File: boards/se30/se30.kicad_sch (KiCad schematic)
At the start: 42 parts, among them J3 Conn_02x05_Odd_Even, U1 ENC624J600-PT, U2 GAL16V8, U3 GAL16V8, U4 SST39SF010, U5 LD1117S33TR_SOT223, Y1 25MHz

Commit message: Rev1 hardware
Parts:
- removed C14: 1uF, Capacitor_SMD:C_0805_2012Metric_Pad1.18x1.45mm_HandSolder, symbol Device:C
- removed U2, U3: GAL16V8, Package_LCC:PLCC-20_THT-Socket, symbol Logic_Programmable:GAL16V8
- added C15 (x4): 1uF, Capacitor_SMD:C_0805_2012Metric_Pad1.18x1.45mm_HandSolder, symbol Device:C
- added H1, H2: MountingHole, MountingHole:MountingHole_5mm, symbol Mechanical:MountingHole
- added J3: Conn_01x07, Connector_PinHeader_2.54mm:PinHeader_1x07_P2.54mm_Vertical, symbol Connector_Generic:Conn_01x07
- added TP1, TP2, TP3, TP4, TP5, TP6: TestPoint, TestPoint:TestPoint_Pad_D1.0mm, symbol Connector:TestPoint
- added U3: 74LVC2G17, Package_TO_SOT_SMD:SOT-363_SC-70-6, symbol 74xGxx:74LVC2G17
- added U4: ATF1502AS-xAx44, Package_QFP:TQFP-44_10x10mm_P0.8mm, symbol CPLD_Microchip:ATF1502AS-xAx44
- C10, C7, C8, C9: Digikey C0805C104M5RAC7800 -> 399-C0805C104M5RAC7800CT-ND; LCSC (none) -> C49678
- C10: renamed from C13; Digikey 293D106X0010A2TE3 -> 718-1118-1-ND; LCSC (none) -> C7171
- C11, C13, C15: Digikey CL21B105KAFNNNE -> 1276-1066-1-ND; LCSC (none) -> C28323
- C12: renamed from C15; Digikey C0805C682K5RAC7800 -> 399-C0805C682K5RAC7800CT-ND; LCSC (none) -> C1755
- C16: renamed from C17; Digikey C0805C103K5RAC7800 -> 399-C0805C103K5RACTUCT-ND; LCSC (none) -> C1710
- C20: renamed from C18; footprint Capacitor_SMD:C_0805_2012Metric_Pad1.18x1.45mm_HandSolder -> Capacitor_SMD:C_1206_3216Metric_Pad1.33x1.80mm_HandSolder; Digikey C0805X102K102T -> 4587-C1206X102K202TCT-ND; LCSC (none) -> C282813
- C22: renamed from C19; Digikey C0805C104M5RAC7800 -> 399-C0805C104M5RAC7800CT-ND; LCSC (none) -> C49678
- C23: renamed from C20; Digikey 293D106X0010A2TE3 -> 718-1118-1-ND; LCSC (none) -> C7171
- C5: renamed from C16; Digikey C0805C103K5RAC7800 -> 399-C0805C103K5RACTUCT-ND; LCSC (none) -> C1710
- C5, C6: Digikey C0805C180K5GAC7800 -> 399-C0805C180K5GAC7800CT-ND; LCSC (none) -> C1797
- C9: renamed from C14; Digikey C0805C682K5RAC7800 -> 399-C0805C682K5RAC7800CT-ND; LCSC (none) -> C1755
- FB1: Digikey CB05YTYH331 -> 240-2549-1-ND; LCSC (none) -> C1015
- J3: Digikey 302-S101 -> ED1543-ND; LCSC (none) -> C17179451
- JP1: renamed from JP2; footprint Jumper:SolderJumper-2_P1.3mm_Open_RoundedPad1.0x1.5mm -> Connector_PinHeader_2.54mm:PinHeader_1x02_P2.54mm_Vertical; now left out of the parts list
- JP2: renamed from JP1; footprint Jumper:SolderJumper-2_P1.3mm_Open_RoundedPad1.0x1.5mm -> Connector_PinHeader_2.54mm:PinHeader_1x02_P2.54mm_Vertical; now left out of the parts list
- R1: Digikey RMCF0805FT12K4 -> RMCF0805FT12K4CT-ND; LCSC (none) -> C317429
- R1, R2: Digikey RMCF0805FT10K0 -> RMCF0805FT10K0CT-ND; LCSC (none) -> C17414
- R2: renamed from R9; Digikey RMCF0805FT49R9 -> RMCF0805FT49R9CT-ND; LCSC (none) -> C17720
- R3: renamed from R2; Digikey RMCF0805FT10K0 -> RMCF0805FT10K0CT-ND; LCSC (none) -> C17414
- R4: renamed from R8; Digikey RMCF0805FT49R9 -> RMCF0805FT49R9CT-ND; LCSC (none) -> C17720
- R5: renamed from R6; Digikey RMCF0805FT49R9 -> RMCF0805FT49R9CT-ND; LCSC (none) -> C17720
- R6: renamed from R7; Digikey RMCF0805FT10R0 -> RMCF0805FT10R0CT-ND; LCSC (none) -> C17415
- R7: renamed from R4; Digikey RMCF0805FT49R9 -> RMCF0805FT49R9CT-ND; LCSC (none) -> C17720
- R8: renamed from R11; Digikey RMCF0805FT75R0 -> RMCF0805FT75R0CT-ND; LCSC (none) -> C2933566
- R9: renamed from R10; Digikey RMCF0805FT75R0 -> RMCF0805FT75R0CT-ND; LCSC (none) -> C2933566
- TR1: LCSC (none) -> C510548
- U2: renamed from U1; LCSC (none) -> C630732
- U4: footprint Package_LCC:PLCC-32_THT-Socket -> Package_SO:TSOP-I-32_14.4x8mm_P0.5mm; symbol Memory_Flash:SST39SF010 -> PDS-Ethernet:SST39SF010-TSOP32; Digikey PLCC-32-AT -> SST39SF010A-70-4C-WHE-ND; Digikey 2 SST39SF010A-55-4C-NHE -> (none); LCSC (none) -> C633793
- U5: Digikey LD1117S33TR -> 497-1242-1-ND; LCSC (none) -> C6186
- Y1: Digikey 2151-RH100-25.000-18-F-1020-EXT-TRDKR-ND -> 2151-RH100-25.000-18-F-1020-EXT-TRCT-ND; LCSC (none) -> C9006
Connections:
- net +3.3V: no longer R3.1
- net +5V: now also U4.8 (VCC), C15.1, C15.1, C15.1, C15.1, J3.5 (Pin_5), U3.5 (VCC), U4.17 (VCC), U4.29 (VCC), U4.41 (VCC), U4.9 (VCC); no longer U4.32 (VCC)
- net A0: now also U4.20 (A0), U4.3 (I/O); no longer U4.12 (A0)
- net A1: now also U4.19 (A1); no longer U4.11 (A1)
- net A10: now also U4.31 (A10); no longer U4.23 (A10)
- net A11: now also U4.1 (A11); no longer U4.25 (A11)
- net A12: now also U4.12 (A12); no longer U4.4 (A12)
- net A13: now also U4.4 (A13); no longer U4.28 (A13)
- net A14: now also U4.5 (A14); no longer U4.29 (A14)
- net A15: now also U4.11 (A15); no longer U4.3 (A15)
- net A16: now also U4.12 (I/O)
- net A2: now also U4.18 (A2); no longer U4.10 (A2)
- net A24: now also U4.13 (I/O)
- net A25: now also U4.14 (I/O)
- net A26: now also U4.15 (I/O)
- net A27: now also U4.18 (I/O)
- net A28: now also U4.19 (I/O/PD2)
- net A29: now also U4.20 (I/O)
- net A3: now also U4.17 (A3); no longer U4.9 (A3)
- net A30: now also U4.21 (I/O)
- net A31: now also U4.22 (I/O)
- net A4: now also U4.16 (A4); no longer U4.8 (A4)
- net A5: now also U4.15 (A5); no longer U4.7 (A5)
- net A6: now also U4.14 (A6); no longer U4.6 (A6)
- net A7: now also U4.13 (A7); no longer U4.5 (A7)
- net A8: now also U4.3 (A8); no longer U4.27 (A8)
- net A9: now also U4.2 (A9); no longer U4.26 (A9)
- net B0SEL: now also TP3.1, U3.3, U4.6 (I/O); no longer U2.50 (WR/WRL/B0SEL/SO)
- net B1SEL: now also TP5.1, U3.1, U4.10 (I/O); no longer U2.48 (WRH/B1SEL)
- net D24: now also U4.21 (D0); no longer U4.13 (D0)
- net D25: now also U4.22 (D1); no longer U4.14 (D1)
- net D26: now also U4.23 (D2); no longer U4.15 (D2)
- net D27: now also U4.25 (D3); no longer U4.17 (D3)
- net D28: now also U4.26 (D4); no longer U4.18 (D4)
- net D29: now also U4.27 (D5); no longer U4.19 (D5)
- net D30: now also U4.28 (D6); no longer U4.20 (D6)
- net D31: now also U4.29 (D7); no longer U4.21 (D7)
- net ETH_CS: now also TP2.1, U4.8 (I/O)
- net ETH_~{INT}: now also U4.11 (I/O)
- net GND: now also JP1.2 (B), JP2.2 (B), R3.1, U4.10 (A16), U4.24 (GND), U4.6 (NC), U4.9 (NC), C15.2, C15.2, C15.2, C15.2, J3.6 (Pin_6), U3.2 (GND), U4.16 (GND), U4.24 (GND), U4.36 (GND), U4.4 (GND); no longer JP1.1 (A), JP2.1 (A), U4.1 (NC), U4.16 (GND), U4.2 (A16), U4.22 (CE)
- net ROM_~{OE}: now also U4.32 (OE), U4.2 (I/O); no longer U4.24 (OE)
- net ROM_~{WE}: now also U4.7 (PGM), U4.5 (I/O/PD1); no longer U4.31 (PGM)
- net R/~{W}: now also U4.28 (I/O)
- net SIZ0: now also U4.25 (I/O)
- net SIZ1: now also U4.27 (I/O)
- net ~{AS}: now also U4.23 (I/O)
- net ~{DSACK0}: now also U4.30 (I/O)
- net ~{DSACK1}: now also U4.31 (I/O)
- net ~{DS}: now also U4.33 (I/O)
- net ~{IRQ1}: now also U4.44 (I/O)
- net ~{IRQ2}: now also U4.43 (I/O)
- net ~{IRQ3}: now also U4.42 (I/O)
- net ~{SLOTID_1}: now reaches R1.2
- net ~{SLOTID_1}: now also JP1.1 (A), U4.37 (I/GCLK1); no longer JP1.2 (B)
- net ~{SLOTID_0}: now reaches R2.2
- net ~{SLOTID_0}: now also JP2.1 (A), U4.35 (I/O/GCLK3); no longer JP2.2 (B)
- net ENC_CLK: now reaches U2.33 (CLKOUT)
- net ENC_CLK: now also U4.40 (I/OE2/GCLK2)
- new net: TP6.1, U4.34 (I/O)
- new net B0SEL': TP1.1, U2.50 (WR/WRL/B0SEL/SO), U3.4
- new net B1SEL': TP4.1, U2.48 (WRH/B1SEL), U3.6
- new net CPLD_VPP: J3.7 (Pin_7), U4.38 (I/OE1/Vpp)
- new net TCK: J3.2 (Pin_2), U4.26 (I/O/TCK)
- new net TDI: J3.3 (Pin_3), U4.1 (I/O/TDI)
- new net TDO: J3.4 (Pin_4), U4.32 (I/O/TDO)
- new net TMS: J3.1 (Pin_1), U4.7 (I/O/TMS)
- new net ~{RESET}: U4.39 (I/GCLR)
- no-connect marks 3 -> 0
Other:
- note removed: "X = open O = closed XX: Slot 9, IRQ 1 XO: Slot E, IRQ 1 OX: Slot A, IRQ 2 XX: Slot B, IRQ 3"
- moved on the sheet: C10, C11, C13, C15, C22, C23, C8, C9, JP1, JP2, R1, R2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

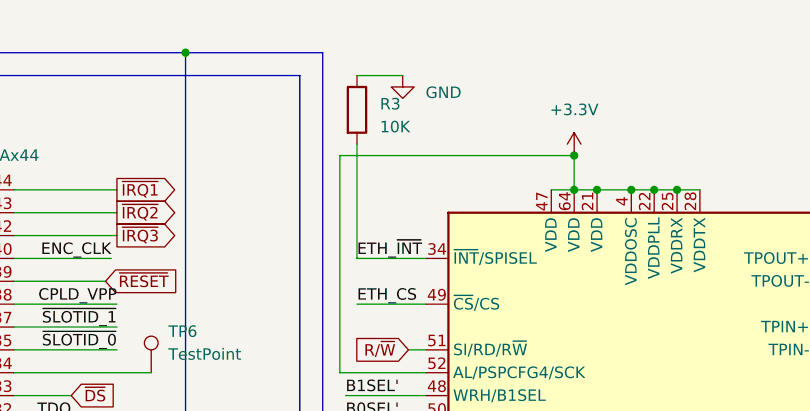
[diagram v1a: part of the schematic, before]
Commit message: SPISEL pulldown resistor should be 100K, not 10K
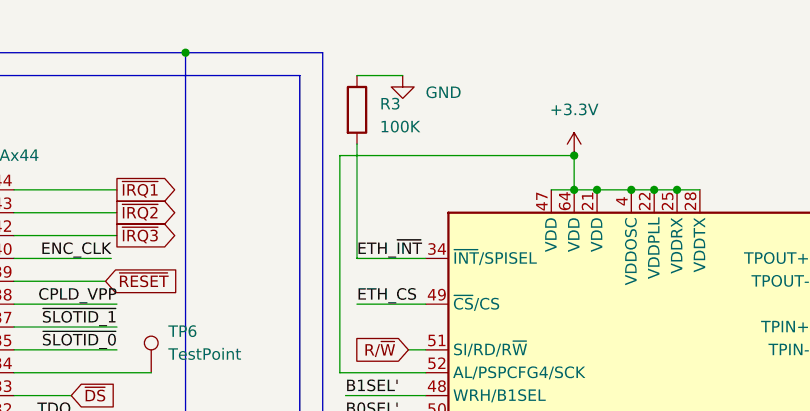
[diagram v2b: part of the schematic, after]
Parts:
- R3: value 10K -> 100K; Digikey RMCF0805FT10K0CT-ND -> (none); LCSC C17414 -> (none)
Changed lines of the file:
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@@
       (effects (font (size 1.27 1.27)) (justify left))
     )
-    (property "Value" "10K" (at 113.03 24.765 0)
+    (property "Value" "100K" (at 113.03 24.765 0)
       (effects (font (size 1.27 1.27)) (justify left))
     )
@@
       (effects (font (size 1.27 1.27)) hide)
     )
-    (property "Digikey" "RMCF0805FT10K0CT-ND" (at 110.49 22.86 0)
+    (property "Digikey" "" (at 110.49 22.86 0)
       (effects (font (size 1.27 1.27)) hide)
     )
-    (property "LCSC" "C17414" (at 110.49 22.86 0)
+    (property "LCSC" "" (at 110.49 22.86 0)
       (effects (font (size 1.27 1.27)) hide)
     )

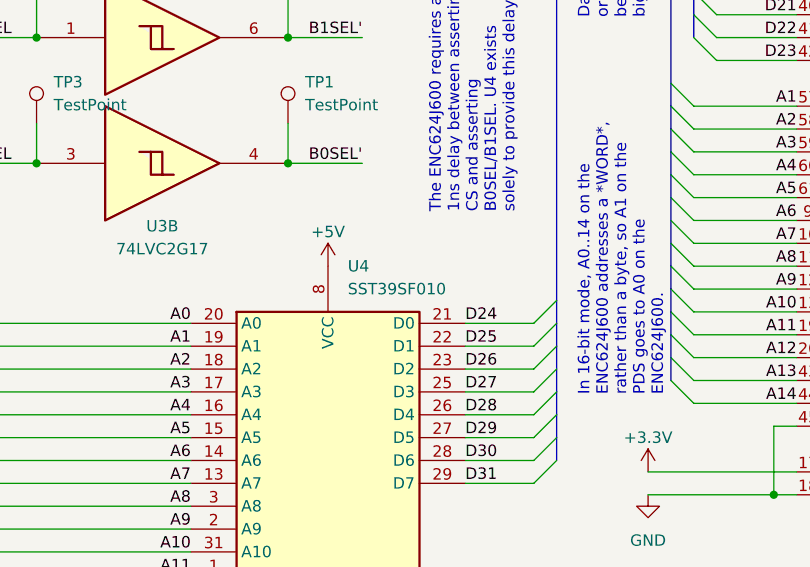
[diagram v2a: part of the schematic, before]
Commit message: Correct footprint for SST39SF010
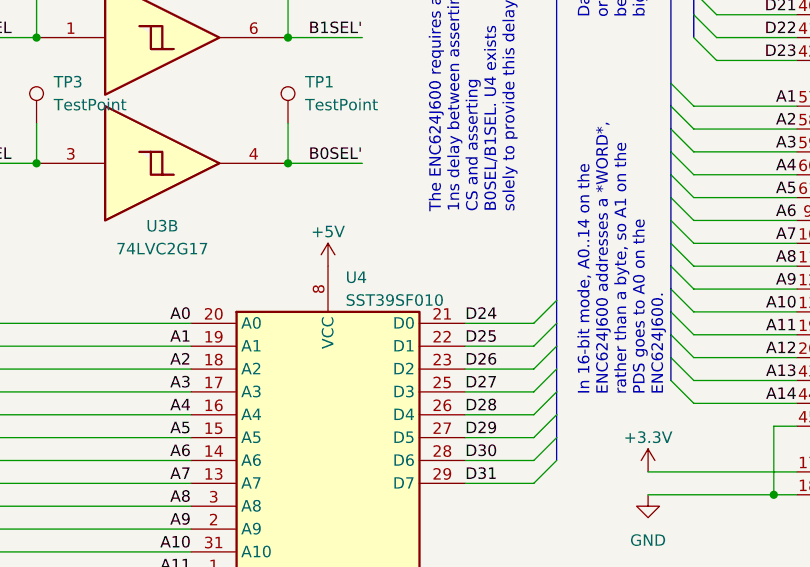
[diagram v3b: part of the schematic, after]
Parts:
- U4: footprint Package_SO:TSOP-I-32_14.4x8mm_P0.5mm -> Package_SO:TSOP-I-32_12.4x8mm_P0.5mm
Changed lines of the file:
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@@
   (symbol (lib_id "PDS-Ethernet:SST39SF010-TSOP32") (at 66.04 160.02 0) (unit 1)
     (in_bom yes) (on_board yes) (dnp no) (fields_autoplaced)
-    (property "Reference" "U4" (at 68.2341 123.19 0)
+    (property "Reference" "U4" (at 67.9959 124.46 0)
       (effects (font (size 1.27 1.27)) (justify left))
     )
-    (property "Value" "SST39SF010" (at 68.2341 125.73 0)
+    (property "Value" "SST39SF010" (at 67.9959 127 0)
       (effects (font (size 1.27 1.27)) (justify left))
     )
-    (property "Footprint" "Package_SO:TSOP-I-32_14.4x8mm_P0.5mm" (at 66.04 152.4 0)
+    (property "Footprint" "Package_SO:TSOP-I-32_12.4x8mm_P0.5mm" (at 66.04 152.4 0)
       (effects (font (size 1.27 1.27)) hide)
     )

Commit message: update schematics
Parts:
- R1, R2: value 10K -> 100K; Digikey RMCF0805FT10K0CT-ND -> RMCF0805FT100KCT-ND; LCSC C17414 -> (none)
- R3: Digikey (none) -> RMCF0805FT100KCT-ND
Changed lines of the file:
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@@
     (effects (font (size 1.27 1.27)) (justify left top))
   )
-  (text_box "The ENC624J600 requires a 1ns delay between asserting CS and asserting B0SEL/B1SEL. U4 exists solely to provide this delay."
-    (at 76.2 86.36 90) (size 11.43 31.75)
+  (text_box "The ENC624J600 requires a 1ns delay between asserting CS and asserting B0SEL/B1SEL. U4 was placed to provide this delay, but it was insufficent, and a feedback through the CPLD provided better results."
+    (at 73.66 86.36 90) (size 13.97 31.75)
     (stroke (width -0.0001) (type default))
     (fill (type none))
@@
       (effects (font (size 1.27 1.27)) hide)
     )
-    (property "Digikey" "" (at 110.49 22.86 0)
+    (property "Digikey" "RMCF0805FT100KCT-ND" (at 110.49 22.86 0)
       (effects (font (size 1.27 1.27)) hide)
     )
@@
       (effects (font (size 1.27 1.27)) (justify left))
     )
-    (property "Value" "10K" (at 193.04 124.46 0)
+    (property "Value" "100K" (at 193.04 124.46 0)
       (effects (font (size 1.27 1.27)) (justify left))
     )
@@
       (effects (font (size 1.27 1.27)) hide)
     )
-    (property "Digikey" "RMCF0805FT10K0CT-ND" (at 191.135 122.555 0)
-      (effects (font (size 1.27 1.27)) hide)
-    )
-    (property "LCSC" "C17414" (at 191.135 122.555 0)
+    (property "Digikey" "RMCF0805FT100KCT-ND" (at 191.135 122.555 0)
+      (effects (font (size 1.27 1.27)) hide)
+    )
+    (property "LCSC" "" (at 191.135 122.555 0)
       (effects (font (size 1.27 1.27)) hide)
     )
@@
       (effects (font (size 1.27 1.27)) (justify right))
     )
-    (property "Value" "10K" (at 184.785 124.46 0)
+    (property "Value" "100K" (at 184.785 124.46 0)
       (effects (font (size 1.27 1.27)) (justify right))
     )
@@
       (effects (font (size 1.27 1.27)) hide)
     )
-    (property "Digikey" "RMCF0805FT10K0CT-ND" (at 187.325 122.555 0)
-      (effects (font (size 1.27 1.27)) hide)
-    )
-    (property "LCSC" "C17414" (at 187.325 122.555 0)
-      (effects (font (size 1.27 1.27)) hide)
-    )
+    (property "Digikey" "RMCF0805FT100KCT-ND" (at 187.325 122.555 0)
+      (effects (font (size 1.27 1.27)) hide)
+    )
+    (property "LCSC" "" (at 187.325 122.555 0)
+      (effects (font (size 1.27 1.27)) hide)
+    )

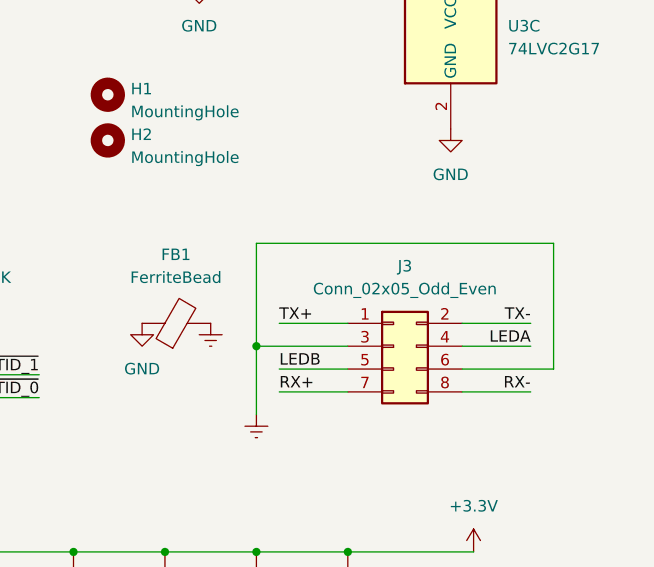
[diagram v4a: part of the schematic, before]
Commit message: SE30: replace vertical breakout connector with right-angle
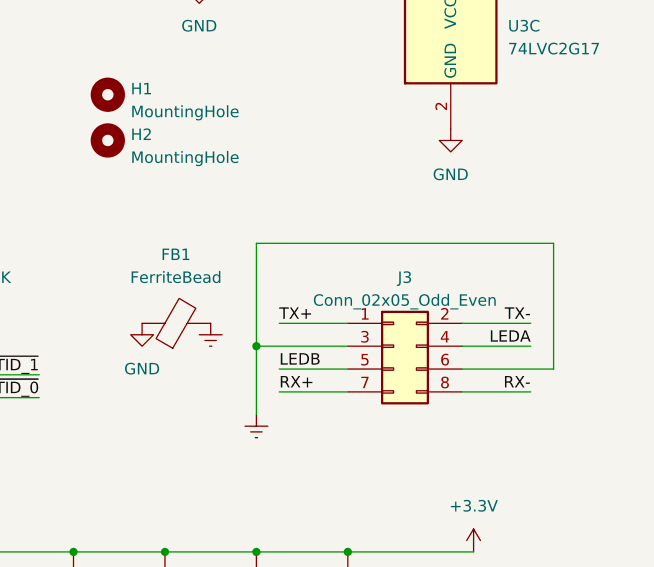
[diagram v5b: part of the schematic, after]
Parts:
- J3: footprint Connector_IDC:IDC-Header_2x04_P2.54mm_Vertical -> Connector_IDC:IDC-Header_2x04_P2.54mm_Horizontal; Digikey ED1543-ND -> 2057-BHR-08-HUA-ND
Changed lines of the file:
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@@
   (symbol (lib_id "Connector_Generic:Conn_02x04_Odd_Even") (at 240.03 132.08 0) (unit 1)
     (in_bom yes) (on_board yes) (dnp no) (fields_autoplaced)
-    (property "Reference" "J3" (at 241.3 123.19 0)
+    (property "Reference" "J3" (at 241.3 124.46 0)
       (effects (font (size 1.27 1.27)))
     )
-    (property "Value" "Conn_02x05_Odd_Even" (at 241.3 125.73 0)
+    (property "Value" "Conn_02x05_Odd_Even" (at 241.3 127 0)
       (effects (font (size 1.27 1.27)))
     )
-    (property "Footprint" "Connector_IDC:IDC-Header_2x04_P2.54mm_Vertical" (at 240.03 132.08 0)
+    (property "Footprint" "Connector_IDC:IDC-Header_2x04_P2.54mm_Horizontal" (at 240.03 132.08 0)
       (effects (font (size 1.27 1.27)) hide)
     )
@@
       (effects (font (size 1.27 1.27)) hide)
     )
-    (property "Digikey" "ED1543-ND" (at 240.03 132.08 0)
+    (property "Digikey" "2057-BHR-08-HUA-ND" (at 240.03 132.08 0)
       (effects (font (size 1.27 1.27)) hide)
     )
